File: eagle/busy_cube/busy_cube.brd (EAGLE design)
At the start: 129.2 x 90.2 mm, 6 parts

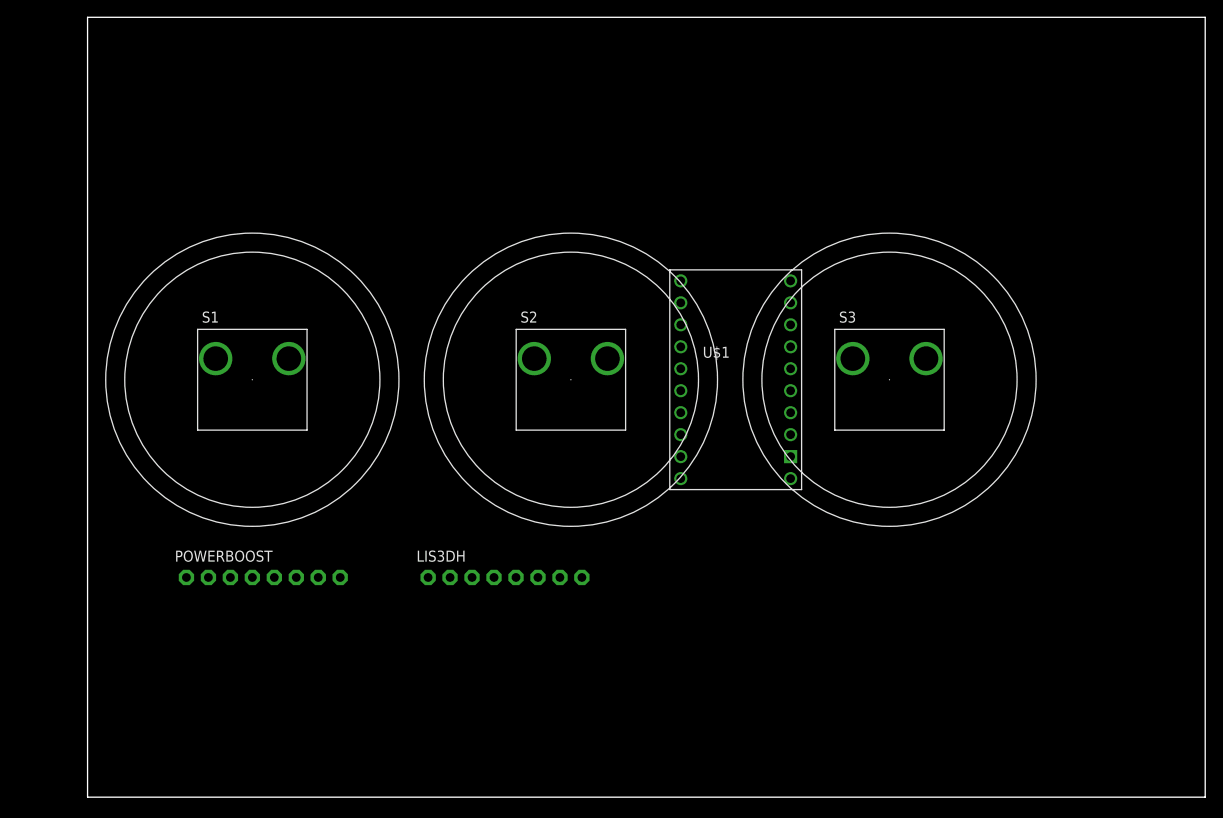
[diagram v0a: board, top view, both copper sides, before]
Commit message: First attempt for wiring
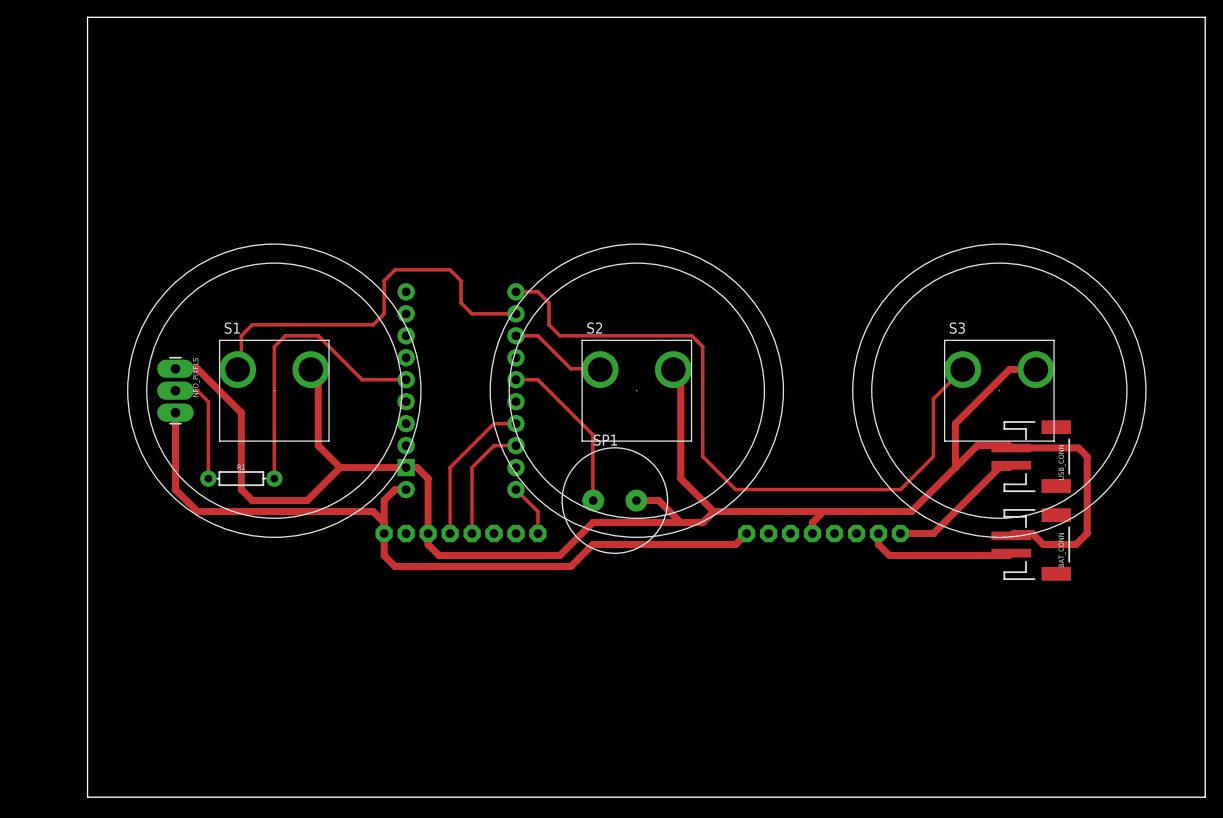
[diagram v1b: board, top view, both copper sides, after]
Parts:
- added BAT_CONN, USB_CONN: (no value), busy_cube_lib:JST-2-SMD
- added NEO_PIXELS: (no value), busy_cube_lib:1X03_LONGPADS
- added R1: 500, busy_cube_lib:AXIAL-0.3
- added SP1: SPEAKER/PS12, busy_cube_lib:PS12
- moved POWERBOOST 65.0 mm to (85.1, 30.5), flipped to the bottom
- moved U$1 31.8 mm to (43.2, 47.0), flipped to the bottom
- moved S3 12.8 mm to (105.4, 47.0)
- moved S2 7.73 mm to (63.5, 47.0)
- moved LIS3DH 7.18 mm to (43.2, 30.5), flipped to the bottom, turned to 180 degrees
- moved S1 2.84 mm to (21.6, 47.0)
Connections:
- removed net VIN: U$1.VIN
- new net BAT_IN_VCC: BAT_CONN.2, POWERBOOST.BAT
- new net BTN1: S1.T, U$1.8
- new net BTN2: S2.T, U$1.7
- new net BTN3: S3.T, U$1.9
- new net N$1: LIS3DH.SCL, U$1.3
- new net N$2: LIS3DH.SDA, U$1.2
- new net N$3: LIS3DH.INT, U$1.0
- new net NEO: R1.P$2, U$1.12
- new net NEO_RES: NEO_PIXELS.2, R1.P$1
- new net SPKR: SP1.P$1, U$1.5
- new net USB_IN_VCC: POWERBOOST.USB, USB_CONN.2
- new net VCC: LIS3DH.VIN, NEO_PIXELS.3, POWERBOOST.5V, U$1.VIN
- net GND: now also BAT_CONN.1, LIS3DH.GND, NEO_PIXELS.1, POWERBOOST.GND, S1.P, S2.P, S3.P, SP1.P$2, USB_CONN.1
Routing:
- net GND: track 0.00 -> 209.1 mm
- net VCC: track 0.00 -> 89.3 mm
- net BTN3: track 0.00 -> 79.7 mm
- net BTN1: track 0.00 -> 44.8 mm
- net NEO: track 0.00 -> 33.1 mm
- net SPKR: track 0.00 -> 19.2 mm
- net N$1: track 0.00 -> 17.3 mm
- net BAT_IN_VCC: track 0.00 -> 17.3 mm
- net USB_IN_VCC: track 0.00 -> 16.1 mm
- net N$2: track 0.00 -> 13.8 mm
- net NEO_RES: track 0.00 -> 13.2 mm
- net BTN2: track 0.00 -> 11.4 mm
- net N$3: track 0.00 -> 6.13 mm
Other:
- board text added: "View from bottom"

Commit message: some more changes
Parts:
- moved NEO_PIXELS 35.9 mm to (5.08, 14.0)
- moved BAT_CONN 27.5 mm to (95.2, 6.35)
- moved USB_CONN 27.5 mm to (95.2, 16.5)
- moved S1 26.2 mm to (8.89, 24.1)
- moved S2 26.2 mm to (50.8, 24.1)
- moved S3 26.2 mm to (92.7, 24.1)
- moved U$1 26.2 mm to (30.5, 24.1)
- moved LIS3DH 26.2 mm to (30.5, 7.62)
- moved POWERBOOST 26.2 mm to (72.4, 7.62)
- moved SP1 26.2 mm to (48.3, 11.4)
- moved R1 20.5 mm to (15.2, 16.5)
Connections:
- net BTN1: now also U$1.11; no longer U$1.8
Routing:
- net BTN1: track 44.8 -> 23.8 mm
- net GND: track 209.1 -> 189.0 mm
- net NEO: track 33.1 -> 13.2 mm
- net VCC: track 89.3 -> 72.3 mm
- net USB_IN_VCC: track 16.1 -> 13.5 mm
- net NEO_RES: track 13.2 -> 10.7 mm
- net BAT_IN_VCC: track 17.3 -> 19.2 mm
- net BTN3: track 79.7 -> 80.4 mm
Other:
- board size 129.2 x 90.2 mm -> 102.9 x 39.4 mm

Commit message: small changes
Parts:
- removed S3: ADA-ARCADE-BTN30MM, busy_cube_lib:ARCADE-BTN-30MM
- added S0: ADA-ARCADE-BTN30MM, busy_cube_lib:ARCADE-BTN-30MM
- moved S1 41.9 mm to (50.8, 24.1)
- moved S2 41.9 mm to (92.7, 24.1)
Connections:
- removed net BTN3: S3.T, U$1.9
- new net BTN0: S0.T, U$1.11
- net BTN1: now also U$1.7; no longer U$1.11
- net BTN2: now also U$1.9; no longer U$1.7
- net GND: now also S0.P; no longer S3.P
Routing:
- net BTN3: track 80.4 -> 0.00 mm
- net BTN2: track 11.4 -> 80.4 mm
- net BTN0: track 0.00 -> 23.8 mm
- net BTN1: track 23.8 -> 11.4 mm
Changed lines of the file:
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@@
 <element name="LIS3DH" library="busy_cube_lib" package="LIS3DH-1X08" value="" x="30.48" y="7.62" rot="MR180"/>
 <element name="POWERBOOST" library="busy_cube_lib" package="POWERBOOST-1X08" value="" x="72.39" y="7.62" rot="MR0"/>
-<element name="S1" library="busy_cube_lib" package="ARCADE-BTN-30MM" value="ADA-ARCADE-BTN30MM" x="8.89" y="24.13"/>
-<element name="S2" library="busy_cube_lib" package="ARCADE-BTN-30MM" value="ADA-ARCADE-BTN30MM" x="50.8" y="24.13"/>
-<element name="S3" library="busy_cube_lib" package="ARCADE-BTN-30MM" value="ADA-ARCADE-BTN30MM" x="92.71" y="24.13"/>
+<element name="S0" library="busy_cube_lib" package="ARCADE-BTN-30MM" value="ADA-ARCADE-BTN30MM" x="8.89" y="24.13"/>
+<element name="S1" library="busy_cube_lib" package="ARCADE-BTN-30MM" value="ADA-ARCADE-BTN30MM" x="50.8" y="24.13"/>
+<element name="S2" library="busy_cube_lib" package="ARCADE-BTN-30MM" value="ADA-ARCADE-BTN30MM" x="92.71" y="24.13"/>
 <element name="U$1" library="busy_cube_lib" package="POLOLU-ASTAR_MICRO_MIN" value="POLOLU-ASTAR-MICROMINIMAL" x="30.48" y="24.13" rot="MR0"/>
 <element name="USB_CONN" library="busy_cube_lib" package="JST-2-SMD" value="" x="95.25" y="16.51" rot="R270">
@@
 <contactref element="U$1" pad="GND"/>
 <contactref element="LIS3DH" pad="GND"/>
-<contactref element="S3" pad="P"/>
 <contactref element="S2" pad="P"/>
 <contactref element="S1" pad="P"/>
+<contactref element="S0" pad="P"/>
 <contactref element="USB_CONN" pad="1"/>
 <contactref element="BAT_CONN" pad="1"/>
@@
 <wire x1="39.37" y1="10.16" x2="36.83" y2="12.7" width="0.4064" layer="1"/>
 </signal>
-<signal name="BTN3">
+<signal name="BTN2">
 <contactref element="U$1" pad="9"/>
-<contactref element="S3" pad="T"/>
+<contactref element="S2" pad="T"/>
 <wire x1="36.83" y1="35.56" x2="39.37" y2="35.56" width="0.4064" layer="1"/>
 <wire x1="39.37" y1="35.56" x2="40.64" y2="34.29" width="0.4064" layer="1"/>
@@
 <wire x1="10.16" y1="11.43" x2="5.08" y2="11.43" width="0.4064" layer="1"/>
 </signal>
-<signal name="BTN2">
-<contactref element="S2" pad="T"/>
+<signal name="BTN1">
+<contactref element="S1" pad="T"/>
 <contactref element="U$1" pad="7"/>
 <wire x1="36.83" y1="30.48" x2="39.37" y2="30.48" width="0.4064" layer="1"/>
@@
 <wire x1="45.72" y1="11.47" x2="45.76" y2="11.43" width="0.4064" layer="1"/>
 </signal>
-<signal name="BTN1">
-<contactref element="S1" pad="T"/>
+<signal name="BTN0">
+<contactref element="S0" pad="T"/>
 <contactref element="U$1" pad="11"/>
 <wire x1="24.13" y1="27.94" x2="19.05" y2="27.94" width="0.4064" layer="1"/>

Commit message: Major changes since I need to switch to SPI with the accelerometer
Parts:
- added R2: 0, busy_cube_lib:1206
- U$1: value POLOLU-ASTAR-MICROMINIMAL -> POLOLU-ASTAR-MICRO; device busy_cube_lib:POLOLU-ASTAR_MICRO_MIN -> busy_cube_lib:POLOLU-ASTAR-MICRO
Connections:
- net NEO renamed N$2
- removed net BTN0: S0.T, U$1.11
- removed net N$2 (its old number): LIS3DH.SDA, U$1.2
- new net N$4: LIS3DH.SDO, U$1.14
- new net N$5: R2.1, U$1.16
- new net N$6: LIS3DH.SCL, U$1.15
- new net N$7: S0.T, U$1.7
- new net N$8: LIS3DH.SDA, R2.2
- net BTN1: now also U$1.2; no longer U$1.7
- net BTN2: now also U$1.3; no longer U$1.9
- net N$1: now also LIS3DH.INT, U$1.1; no longer LIS3DH.SCL, U$1.3
- net N$3: now also LIS3DH.CS; no longer LIS3DH.INT
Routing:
- net N$7: track 0.00 -> 47.4 mm
- net BTN0: track 23.8 -> 0.00 mm
- net SPKR: track 19.2 -> 0.00 mm
- net N$2 (its old number): track 13.8 -> 0.00 mm
- net N$5: track 0.00 -> 13.1 mm
- net N$1: track 17.3 -> 9.42 mm
- net BTN1: track 11.4 -> 17.4 mm
- net N$6: track 0.00 -> 5.61 mm
- net N$4: track 0.00 -> 5.61 mm
- net BTN2: track 80.4 -> 85.5 mm
- net N$8: track 0.00 -> 3.01 mm
- net GND: track 189.0 -> 188.3 mm

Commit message: PCB changes
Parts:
- added EXT_SWITCH: (no value), busy_cube_lib:JST-2-SMD
- added R3: 300, busy_cube_lib:AXIAL-0.3
- moved NEO_PIXELS 12.8 mm to (3.81, 26.7)
- moved POWERBOOST 6.35 mm to (77.5, 11.4)
- moved S2 5.08 mm to (97.8, 24.1)
- moved S1 5.08 mm to (55.9, 24.1)
- moved SP1 5.08 mm to (53.3, 11.4)
- moved LIS3DH 5.08 mm to (35.6, 7.62)
- moved U$1 5.08 mm to (35.6, 24.1)
- moved R1 5.08 mm to (20.3, 16.5)
- moved S0 5.08 mm to (14.0, 24.1)
- moved BAT_CONN 5.08 mm to (100.3, 6.35)
- moved R2 5.08 mm to (39.4, 10.2)
- moved USB_CONN 5.08 mm to (100.3, 16.5)
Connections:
- new net N$10: BAT_CONN.2, EXT_SWITCH.1
- new net N$9: R3.P$2, SP1.P$1
- net BAT_IN_VCC: now also EXT_SWITCH.2; no longer BAT_CONN.2
- net SPKR: now also R3.P$1; no longer SP1.P$1
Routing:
- net N$10: track 0.00 -> 14.9 mm
- net VCC: track 72.3 -> 85.6 mm
- net BAT_IN_VCC: track 19.2 -> 5.92 mm
- net N$9: track 0.00 -> 8.19 mm
- net NEO_RES: track 10.7 -> 16.6 mm
- net SPKR: track 0.00 -> 5.61 mm
- net BTN2: track 85.5 -> 80.9 mm
- net GND: track 188.3 -> 185.5 mm
- net USB_IN_VCC: track 13.5 -> 12.4 mm
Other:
- board size 102.9 x 39.4 mm -> 108 x 39.4 mm

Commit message: PCB changes
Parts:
- moved R1 10.2 mm to (25.4, 25.4), turned to 90 degrees
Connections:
- removed net N$7: S0.T, U$1.7
- new net N$11: S0.P, U$1.7
- net GND: now also S0.T; no longer S0.P
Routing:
- net N$7: track 47.4 -> 0.00 mm
- net N$11: track 0.00 -> 37.9 mm
- net N$2: track 13.2 -> 5.39 mm
- net NEO_RES: track 16.6 -> 22.6 mm
- net GND: track 185.5 -> 182.7 mm
- net VCC: track 85.6 -> 87.8 mm
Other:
- outline, holes or cut-outs redrawn

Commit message: PCB changes
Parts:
- moved U$1 3.81 mm to (35.6, 27.9)
- moved R2 3.81 mm to (39.4, 14.0)
- moved R3 3.81 mm to (45.7, 22.9)
- moved LIS3DH 2.54 mm to (35.6, 10.2)
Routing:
- net GND: track 182.7 -> 178.4 mm
- net N$9: track 8.19 -> 12.0 mm
- net BTN2: track 80.9 -> 77.1 mm
- net BTN1: track 17.4 -> 13.6 mm
- net N$11: track 37.9 -> 39.5 mm
- net VCC: track 87.8 -> 86.2 mm
- net N$2: track 5.39 -> 3.81 mm
- net N$4: track 5.61 -> 7.09 mm
- net N$6: track 5.61 -> 6.88 mm
- net N$3: track 6.13 -> 7.40 mm
- net N$1: track 9.42 -> 10.7 mm
- net N$8: track 3.01 -> 4.28 mm
- net N$5: track 13.1 -> 13.8 mm
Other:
- board size 108 x 39.4 mm -> 108 x 41.9 mm
